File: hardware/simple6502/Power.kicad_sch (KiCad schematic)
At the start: 20 parts, among them J5 POWER 5V, J6 AUX 5VDC, SW2 POWER, U5 74HCT00, U6 74LS30

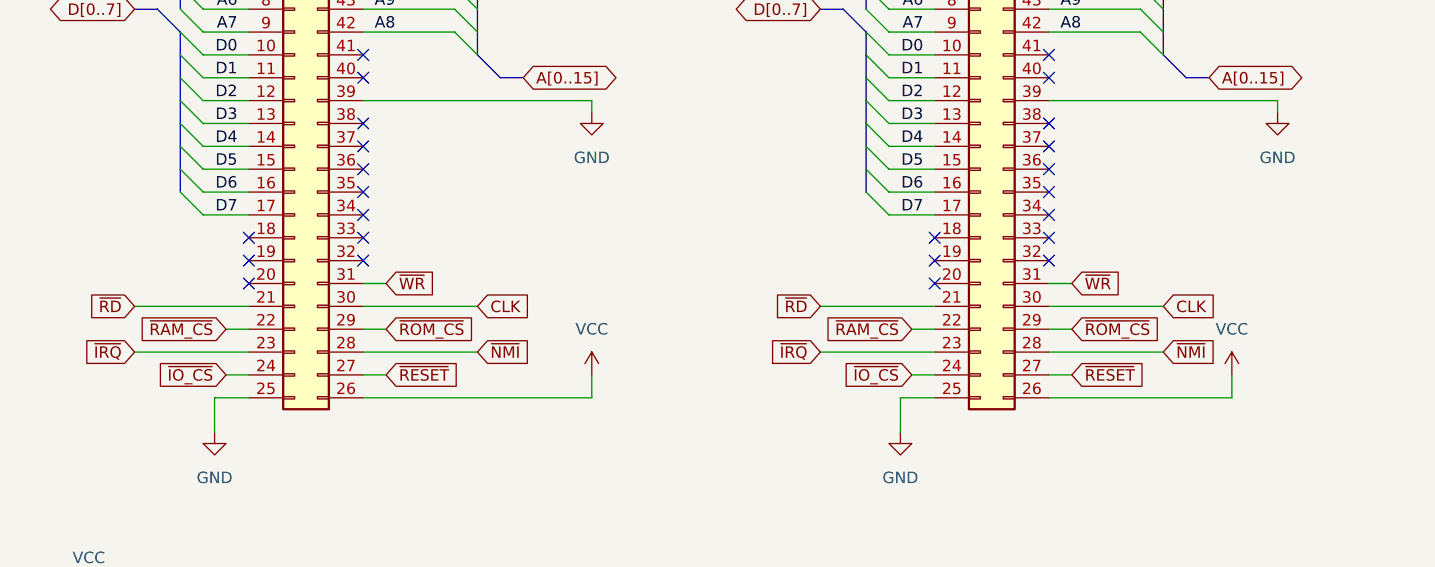
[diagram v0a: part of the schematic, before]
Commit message: more pin rearrangment in bus connector
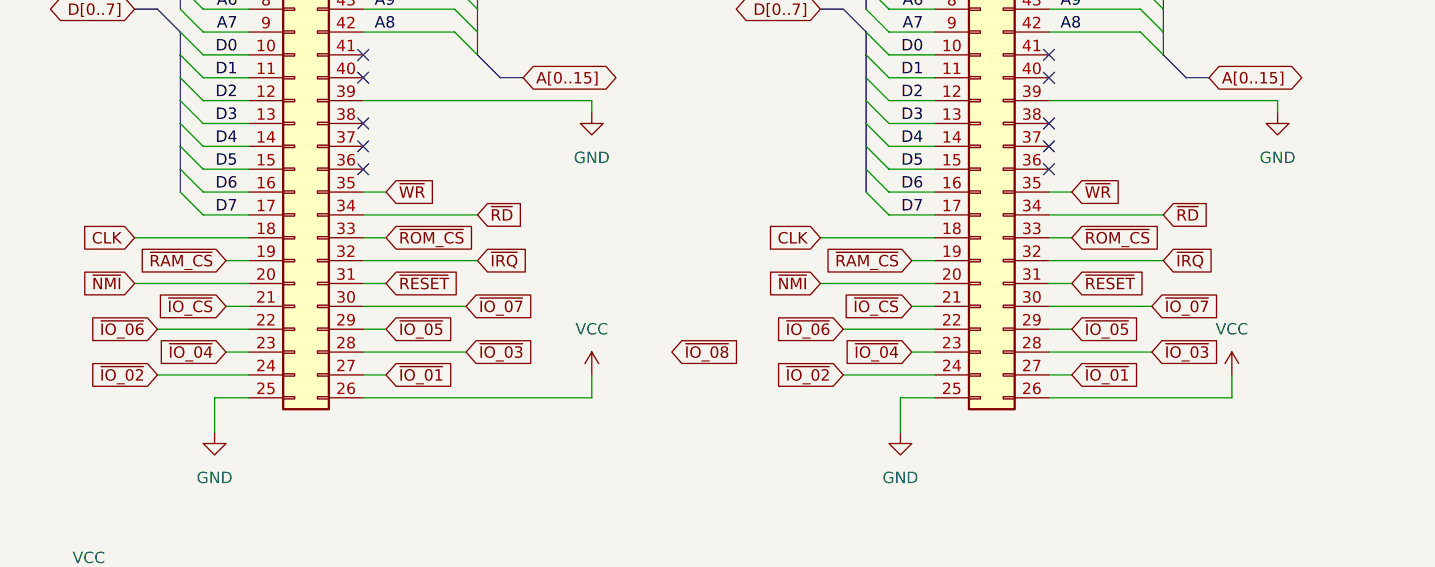
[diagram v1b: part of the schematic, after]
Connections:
- net CLK: now also SLOT1.18 (Pin_18), SLOT2.18 (Pin_18); no longer SLOT1.30 (Pin_30), SLOT2.30 (Pin_30)
- net ~{IO_CS}: now also SLOT1.21 (Pin_21), SLOT2.21 (Pin_21); no longer SLOT1.24 (Pin_24), SLOT2.24 (Pin_24)
- net ~{IRQ}: now also SLOT1.32 (Pin_32), SLOT2.32 (Pin_32); no longer SLOT1.23 (Pin_23), SLOT2.23 (Pin_23)
- net ~{NMI}: now also SLOT1.20 (Pin_20), SLOT2.20 (Pin_20); no longer SLOT1.28 (Pin_28), SLOT2.28 (Pin_28)
- net ~{RAM_CS}: now also SLOT1.19 (Pin_19), SLOT2.19 (Pin_19); no longer SLOT1.22 (Pin_22), SLOT2.22 (Pin_22)
- net ~{RD}: now also SLOT1.34 (Pin_34), SLOT2.34 (Pin_34); no longer SLOT1.21 (Pin_21), SLOT2.21 (Pin_21)
- net ~{RESET}: now also SLOT1.31 (Pin_31), SLOT2.31 (Pin_31); no longer SLOT1.27 (Pin_27), SLOT2.27 (Pin_27)
- net ~{ROM_CS}: now also SLOT1.33 (Pin_33), SLOT2.33 (Pin_33); no longer SLOT1.29 (Pin_29), SLOT2.29 (Pin_29)
- net ~{WR}: now also SLOT1.35 (Pin_35), SLOT2.35 (Pin_35); no longer SLOT1.31 (Pin_31), SLOT2.31 (Pin_31)
- new net ~{IO_01}: SLOT1.27 (Pin_27), SLOT2.27 (Pin_27)
- new net ~{IO_02}: SLOT1.24 (Pin_24), SLOT2.24 (Pin_24)
- new net ~{IO_03}: SLOT1.28 (Pin_28), SLOT2.28 (Pin_28)
- new net ~{IO_04}: SLOT1.23 (Pin_23), SLOT2.23 (Pin_23)
- new net ~{IO_05}: SLOT1.29 (Pin_29), SLOT2.29 (Pin_29)
- new net ~{IO_06}: SLOT1.22 (Pin_22), SLOT2.22 (Pin_22)
- new net ~{IO_07}: SLOT1.30 (Pin_30), SLOT2.30 (Pin_30)
- no-connect marks 26 -> 12

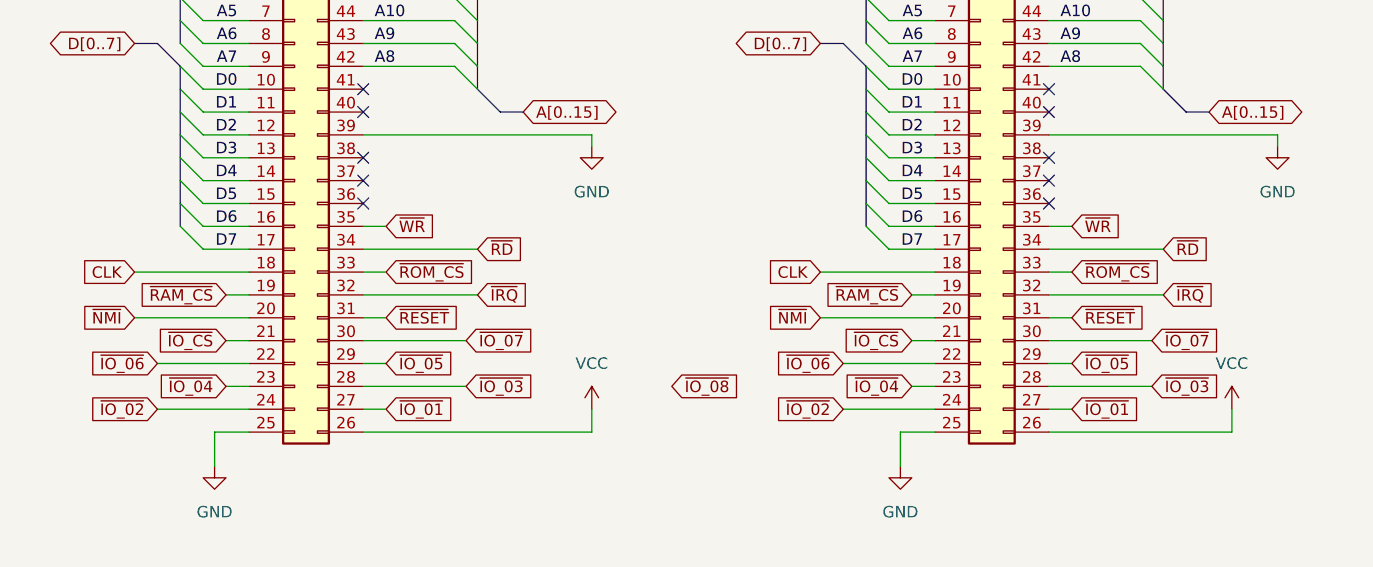
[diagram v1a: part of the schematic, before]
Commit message: Routing v1 finished - DRC passed
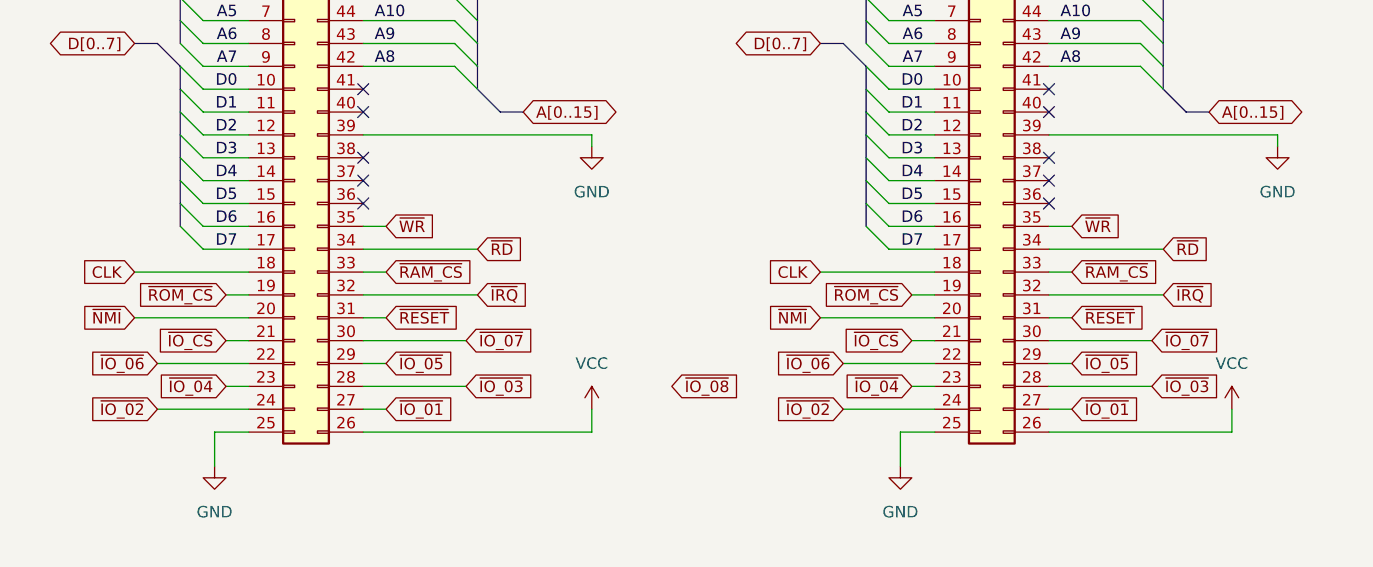
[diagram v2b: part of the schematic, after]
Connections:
- net ~{RAM_CS}: now also SLOT1.33 (Pin_33), SLOT2.33 (Pin_33); no longer SLOT1.19 (Pin_19), SLOT2.19 (Pin_19)
- net ~{ROM_CS}: now also SLOT1.19 (Pin_19), SLOT2.19 (Pin_19); no longer SLOT1.33 (Pin_33), SLOT2.33 (Pin_33)
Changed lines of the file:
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@@
+    )
+  )
+  (global_label "~{ROM_CS}" (shape input) (at 36.83 130.81 180) (fields_autoplaced)
+    (effects (font (size 1.27 1.27)) (justify right))
+    (property "Intersheetrefs" "${INTERSHEET_REFS}" (at 26.3458 130.81 0)
+      (effects (font (size 1.27 1.27)) (justify right) hide)
     )
   )
@@
     )
   )
+  (global_label "~{ROM_CS}" (shape input) (at 113.03 130.81 180) (fields_autoplaced)
+    (effects (font (size 1.27 1.27)) (justify right))
+    (property "Intersheetrefs" "${INTERSHEET_REFS}" (at 102.5458 130.81 0)
+      (effects (font (size 1.27 1.27)) (justify right) hide)
+    )
+  )
   (global_label "~{IO_07}" (shape input) (at 63.5 135.89 0) (fields_autoplaced)
     (effects (font (size 1.27 1.27)) (justify left))
     (property "Intersheetrefs" "${INTERSHEET_REFS}" (at 71.8071 135.89 0)
       (effects (font (size 1.27 1.27)) (justify left) hide)
-    )
-  )
-  (global_label "~{RAM_CS}" (shape input) (at 36.83 130.81 180) (fields_autoplaced)
-    (effects (font (size 1.27 1.27)) (justify right))
-    (property "Intersheetrefs" "${INTERSHEET_REFS}" (at 26.5877 130.81 0)
-      (effects (font (size 1.27 1.27)) (justify right) hide)
     )
   )
@@
     (property "Intersheetrefs" "${INTERSHEET_REFS}" (at 20.1167 128.27 0)
       (effects (font (size 1.27 1.27)) (justify right) hide)
-    )
-  )
-  (global_label "~{ROM_CS}" (shape input) (at 54.61 128.27 0) (fields_autoplaced)
-    (effects (font (size 1.27 1.27)) (justify left))
-    (property "Intersheetrefs" "${INTERSHEET_REFS}" (at 65.0942 128.27 0)
-      (effects (font (size 1.27 1.27)) (justify left) hide)
     )
   )
@@
     (effects (font (size 1.27 1.27)) (justify left))
     (property "Intersheetrefs" "${INTERSHEET_REFS}" (at 62.9171 143.51 0)
-      (effects (font (size 1.27 1.27)) (justify left) hide)
-    )
-  )
-  (global_label "~{ROM_CS}" (shape input) (at 130.81 128.27 0) (fields_autoplaced)
-    (effects (font (size 1.27 1.27)) (justify left))
-    (property "Intersheetrefs" "${INTERSHEET_REFS}" (at 141.2942 128.27 0)
       (effects (font (size 1.27 1.27)) (justify left) hide)
     )
@@
     )
   )
+  (global_label "~{RAM_CS}" (shape input) (at 54.61 128.27 0) (fields_autoplaced)
+    (effects (font (size 1.27 1.27)) (justify left))
+    (property "Intersheetrefs" "${INTERSHEET_REFS}" (at 64.8523 128.27 0)
+      (effects (font (size 1.27 1.27)) (justify left) hide)
+    )
+  )
   (global_label "~{IO_05}" (shape input) (at 54.61 138.43 0) (fields_autoplaced)
     (effects (font (size 1.27 1.27)) (justify left))
@@
     )
   )
-  (global_label "~{RAM_CS}" (shape input) (at 113.03 130.81 180) (fields_autoplaced)
-    (effects (font (size 1.27 1.27)) (justify right))
-    (property "Intersheetrefs" "${INTERSHEET_REFS}" (at 102.7877 130.81 0)
-      (effects (font (size 1.27 1.27)) (justify right) hide)
-    )
-  )
   (global_label "~{IO_07}" (shape input) (at 139.7 135.89 0) (fields_autoplaced)
     (effects (font (size 1.27 1.27)) (justify left))
@@
       (effects (font (size 1.27 1.27)) (justify left) hide)
     )
+  )
+  (global_label "~{RAM_CS}" (shape input) (at 130.81 128.27 0) (fields_autoplaced)
+    (effects (font (size 1.27 1.27)) (justify left))
+    (property "Intersheetrefs" "${INTERSHEET_REFS}" (at 141.0523 128.27 0)
+      (effects (font (size 1.27 1.27)) (justify left) hide)
+    )

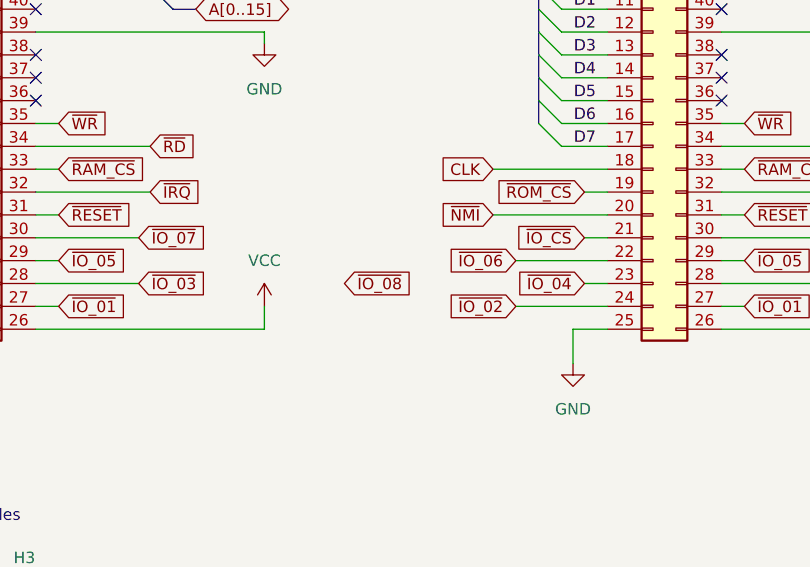
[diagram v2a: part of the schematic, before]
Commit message: Schematics updated to v1 - ERC passed
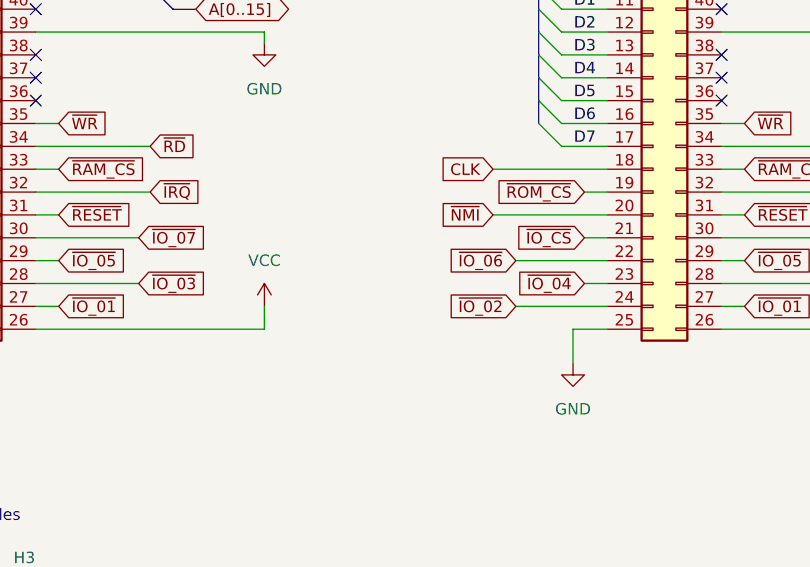
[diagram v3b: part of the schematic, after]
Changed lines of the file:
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@@
   (title_block
     (title "simple6502")
-    (date "2023-09-23")
-    (rev "0.5")
+    (date "2023-09-25")
+    (rev "1.0")
     (company "Mariano Luna")
   )
@@
       (effects (font (size 1.27 1.27)) (justify left) hide)
     )
-  )
-  (global_label "~{IO_08}" (shape input) (at 86.36 140.97 0) (fields_autoplaced)
-    (effects (font (size 1.27 1.27)) (justify left))
-    (property "Intersheetrefs" "${INTERSHEET_REFS}" (at 94.6671 140.97 0)
-      (effects (font (size 1.27 1.27)) (justify left) hide)
-    )

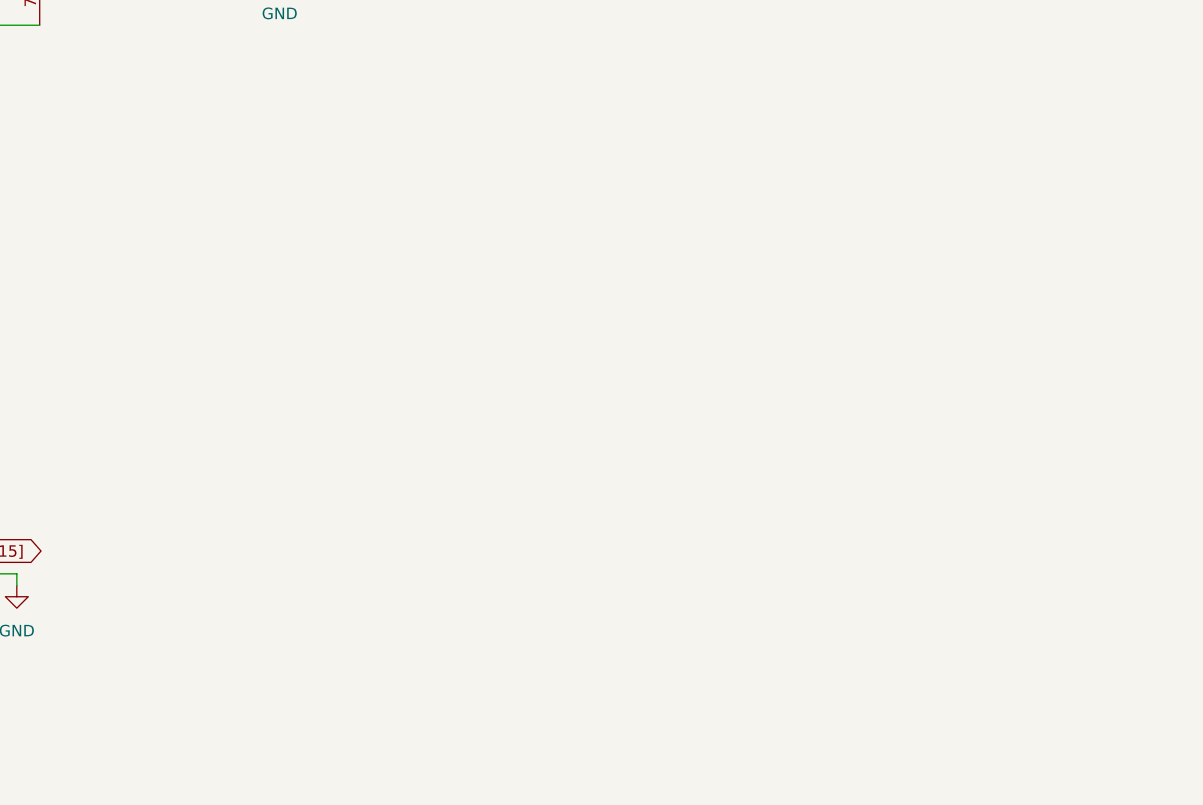
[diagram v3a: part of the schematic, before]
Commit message: Relocated reset
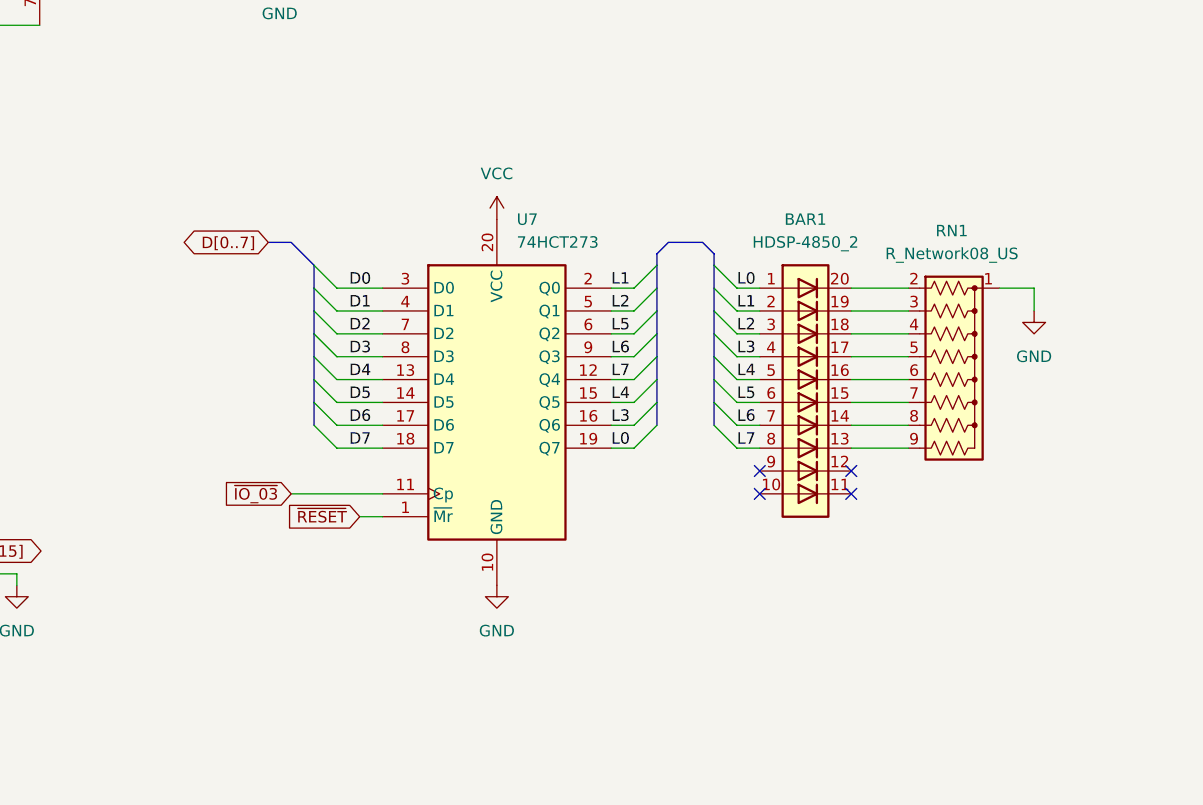
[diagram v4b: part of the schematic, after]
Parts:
- added BAR1: HDSP-4850_2, Display:HDSP-4850, symbol LED:HDSP-4850_2
- added RN1: R_Network08_US, Resistor_THT:R_Array_SIP9, symbol Device:R_Network08_US
- added U7: 74HCT273, Package_DIP:DIP-20_W7.62mm_Socket, symbol 74xx:74HCT273
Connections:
- net D0: now also U7.3 (D0)
- net D1: now also U7.4 (D1)
- net D2: now also U7.7 (D2)
- net D3: now also U7.8 (D3)
- net D4: now also U7.13 (D4)
- net D5: now also U7.14 (D5)
- net D6: now also U7.17 (D6)
- net D7: now also U7.18 (D7)
- net GND: now also RN1.1 (common), U7.10 (GND)
- net VCC: now also U7.20 (VCC)
- net ~{IO_03}: now also U7.11 (Cp)
- net ~{RESET}: now also U7.1 (~{Mr})
- new net: BAR1.20 (K), RN1.2 (R1)
- new net: BAR1.19 (K), RN1.3 (R2)
- new net: BAR1.18 (K), RN1.4 (R3)
- new net: BAR1.17 (K), RN1.5 (R4)
- new net: BAR1.16 (K), RN1.6 (R5)
- new net: BAR1.15 (K), RN1.7 (R6)
- new net: BAR1.14 (K), RN1.8 (R7)
- new net: BAR1.13 (K), RN1.9 (R8)
- new net L0: BAR1.1 (A), U7.19 (Q7)
- new net L1: BAR1.2 (A), U7.2 (Q0)
- new net L2: BAR1.3 (A), U7.5 (Q1)
- new net L3: BAR1.4 (A), U7.16 (Q6)
- new net L4: BAR1.5 (A), U7.15 (Q5)
- new net L5: BAR1.6 (A), U7.6 (Q2)
- new net L6: BAR1.7 (A), U7.9 (Q3)
- new net L7: BAR1.8 (A), U7.12 (Q4)
- no-connect marks 12 -> 16
